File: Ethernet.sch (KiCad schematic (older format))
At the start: 2 parts, among them J2 RJMG2012211A0FR, U4 DP83869HMRGZT

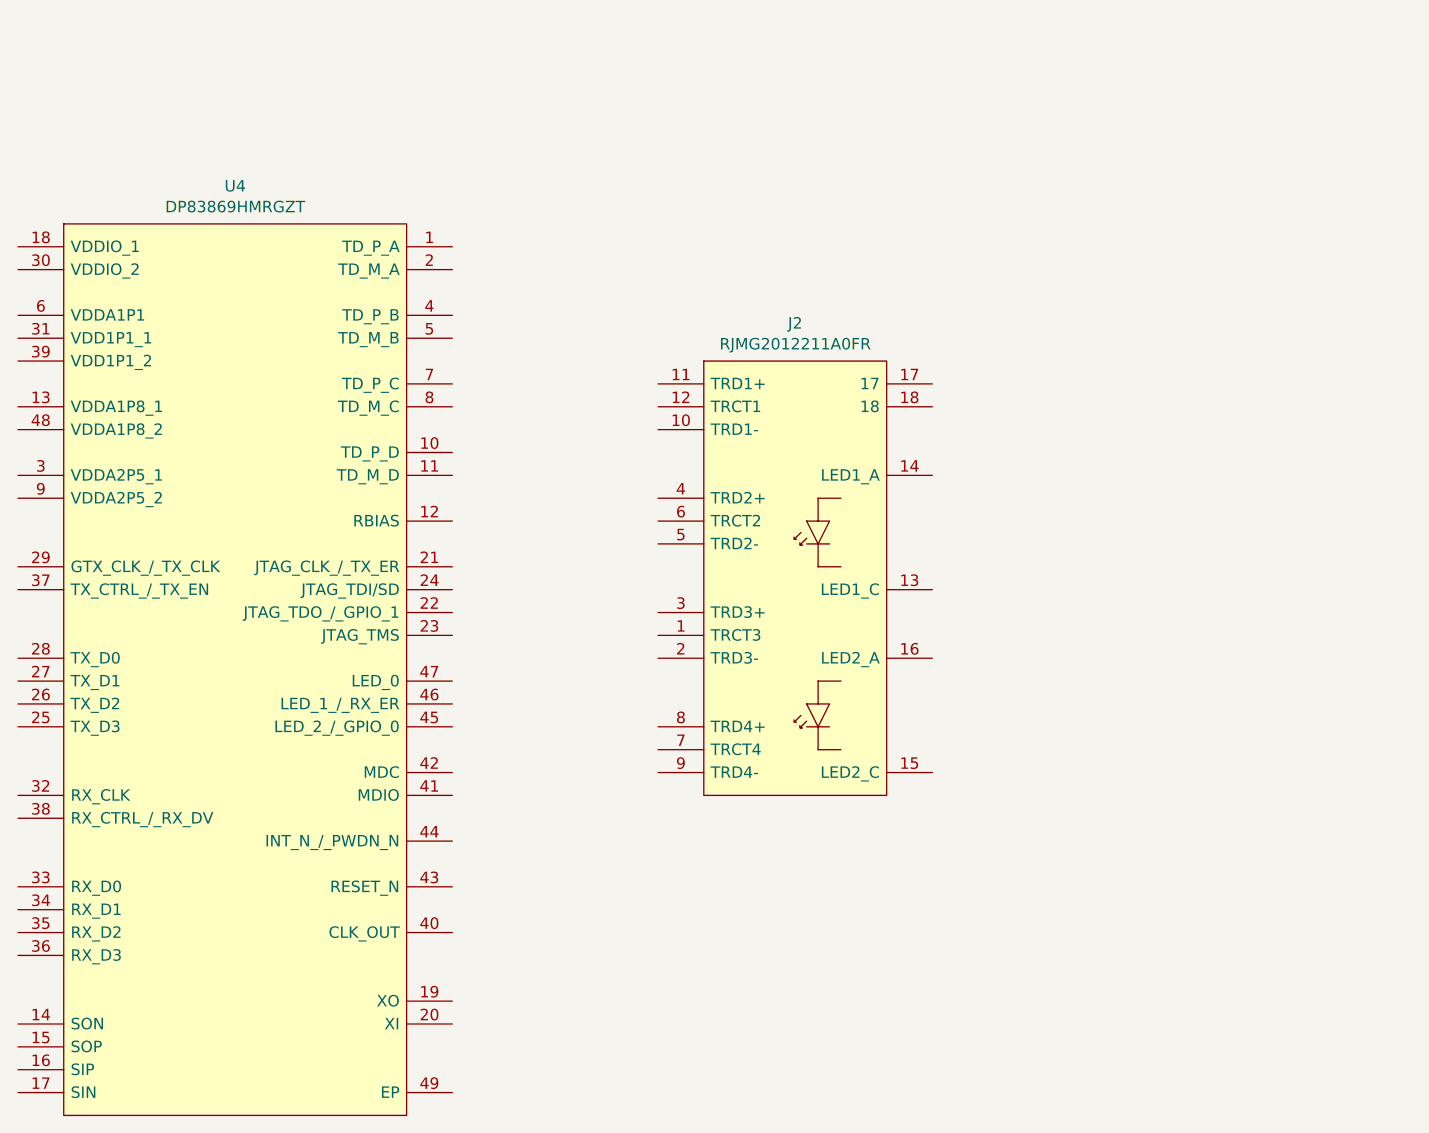
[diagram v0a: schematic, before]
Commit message: Added new sheet for Ethernet PHY Connector and drawn schematic (continue)
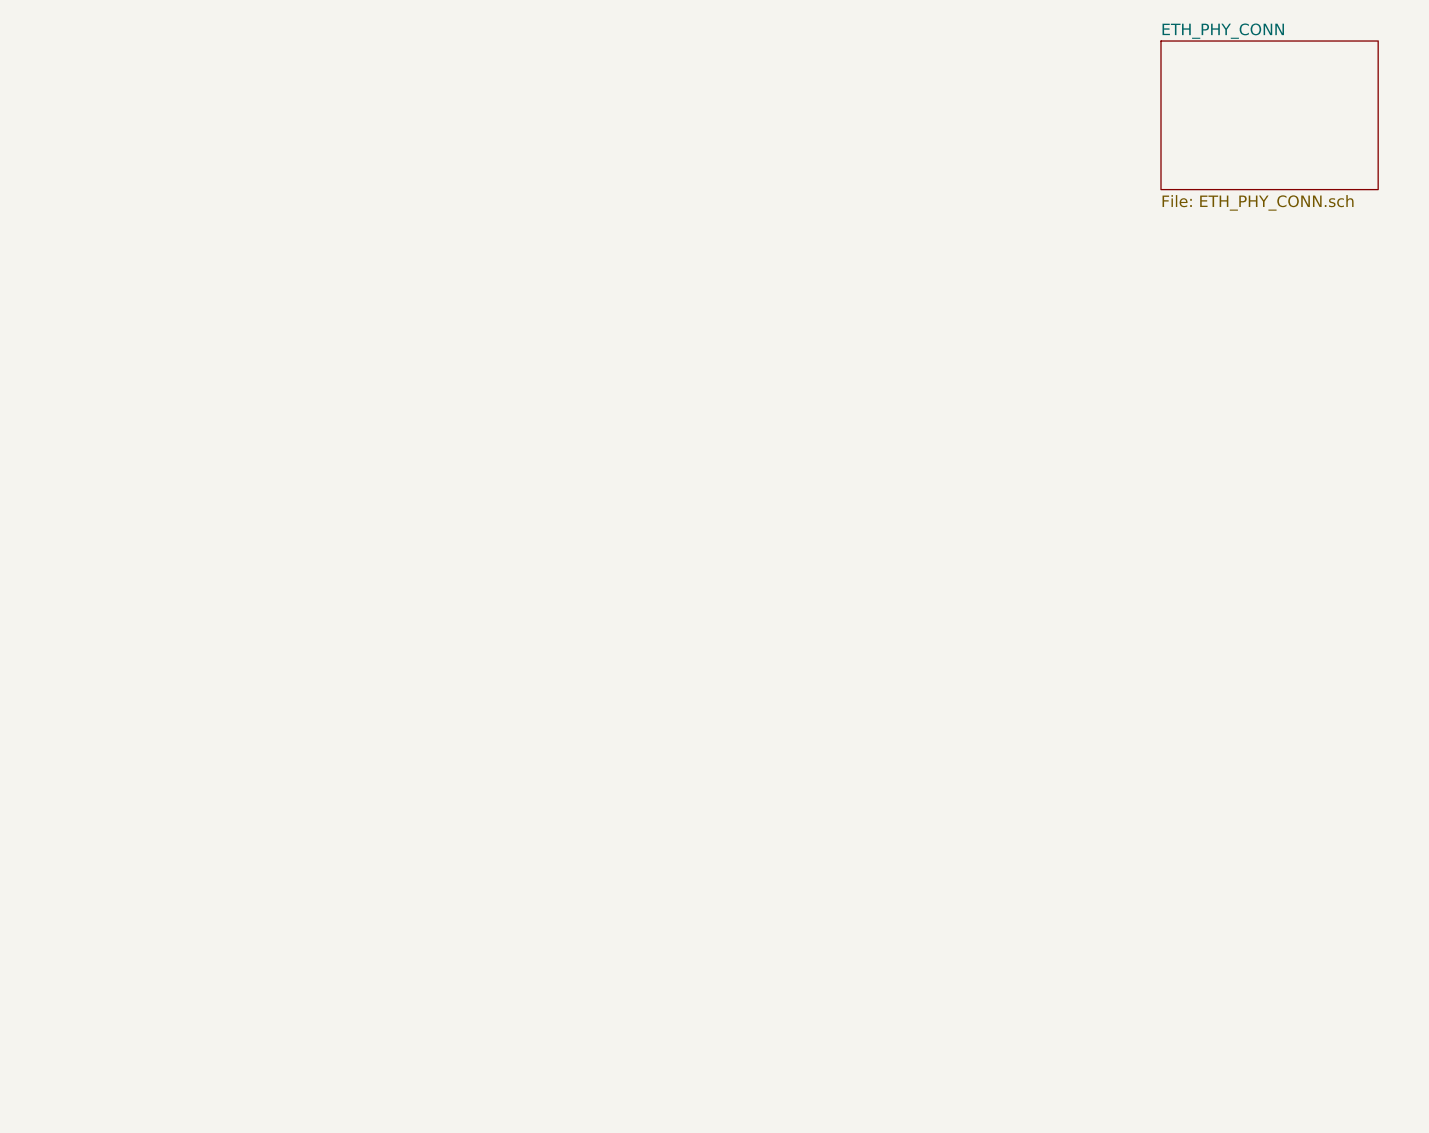
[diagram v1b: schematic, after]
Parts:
- removed J2: RJMG2012211A0FR, Connector_RJ:RJ45_Amphenol_RJMG2012211A0FR, symbol GM_Connectors:RJMG2012211A0FR
- removed U4: DP83869HMRGZT, QFN50P700X700X100-49N-D, symbol GM_Interface_IC:DP83869HMRGZT
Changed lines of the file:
@@
 $Descr A4 11693 8268
 encoding utf-8
-Sheet 11 14
+Sheet 11 15
 Title "CGMPCX1006"
 Date "2021-02-03"
@@
 Comment4 ""
 $EndDescr
-$Comp
-L GM_Connectors:RJMG2012211A0FR J2
-U 1 1 601C9357
-P 7900 2300
-F 0 "J2" H 8300 2465 50  0000 C CNN
-F 1 "RJMG2012211A0FR" H 8300 2374 50  0000 C CNN
-F 2 "Connector_RJ:RJ45_Amphenol_RJMG2012211A0FR" H 9650 2000 50  0001 L CNN
-F 3 "https://cdn.amphenol-icc.com/media/wysiwyg/files/drawing/rjmg2012211a0fr.pdf?__cf_chl_jschl_tk__=5cc0c62f4c4dd1ea6123210829694b2e9dccd0ec-1611686655-0-AbgBvwWp3czzY2TJ0ufJlAIwRl1VXRL4dc53SNg87JU7ShGwndvQnogLdV7Mq2dYunHoQquHJsd7cqqgMDrOCuNnWSljlLOxvZjuWQhC782DzE7hT4o80MjFt4sxGI4f_TcHgfVPuhccmcslPxq7SFrSDqxMMzQN2LDgsyEn_3ccqG3s2uHOZ2TkEeirzi6FrStejh0zz-mYYMOJCy1xpbmAF_0CAQpDLdH_WiZpwToopGmberC5N0wyHm6XbfAZEGelJSep-OdlFNMkB6nmqKb8TAkP2NiiS7GCJMgfNu5ZBovHLyUKdEt6EilXMFd55og80AbueHGldAWIFm-2Z3bJPHamRmYij0aInI9IGAYpuaLA_0nT0TMWXQY6i8JB94etuVIFkjYSa3PI-kWldruV9iNZxoLQLwTfUrN2H5nslIXfuzo0o-iOBHlw1zAeiQ" H 7250 3500 50  0001 L CNN
-	1    7900 2300
-	1    0    0    -1
-$EndComp
-$Comp
-L GM_Interface_IC:DP83869HMRGZT U4
-U 1 1 601CAF41
-P 5100 1700
-F 0 "U4" H 5850 1865 50  0000 C CNN
-F 1 "DP83869HMRGZT" H 5850 1774 50  0000 C CNN
-F 2 "QFN50P700X700X100-49N-D" H 8650 800 50  0001 L CNN
-F 3 "http://www.ti.com/lit/gpn/DP83869HM" H 8650 700 50  0001 L CNN
-	1    5100 1700
-	1    0    0    -1
-$EndComp
+$Sheet
+S 9900 900  950  650
+U 60257FE5
+F0 "ETH_PHY_CONN" 50
+F1 "ETH_PHY_CONN.sch" 50
+$EndSheet
 $EndSCHEMATC

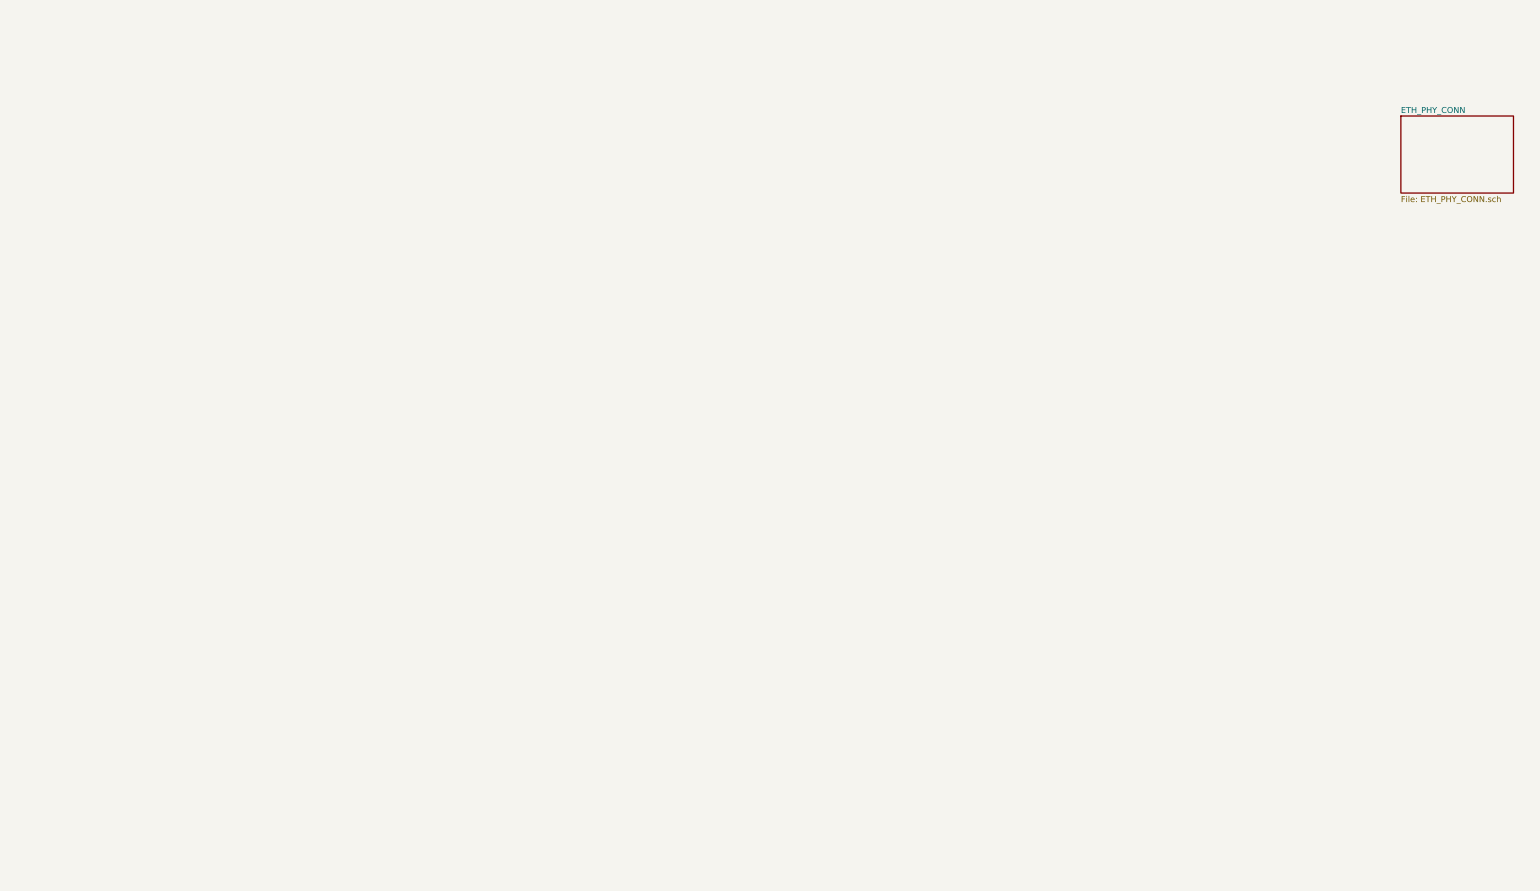
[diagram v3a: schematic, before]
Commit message: Drawn Eth power schematics and Eth PHY (continue)
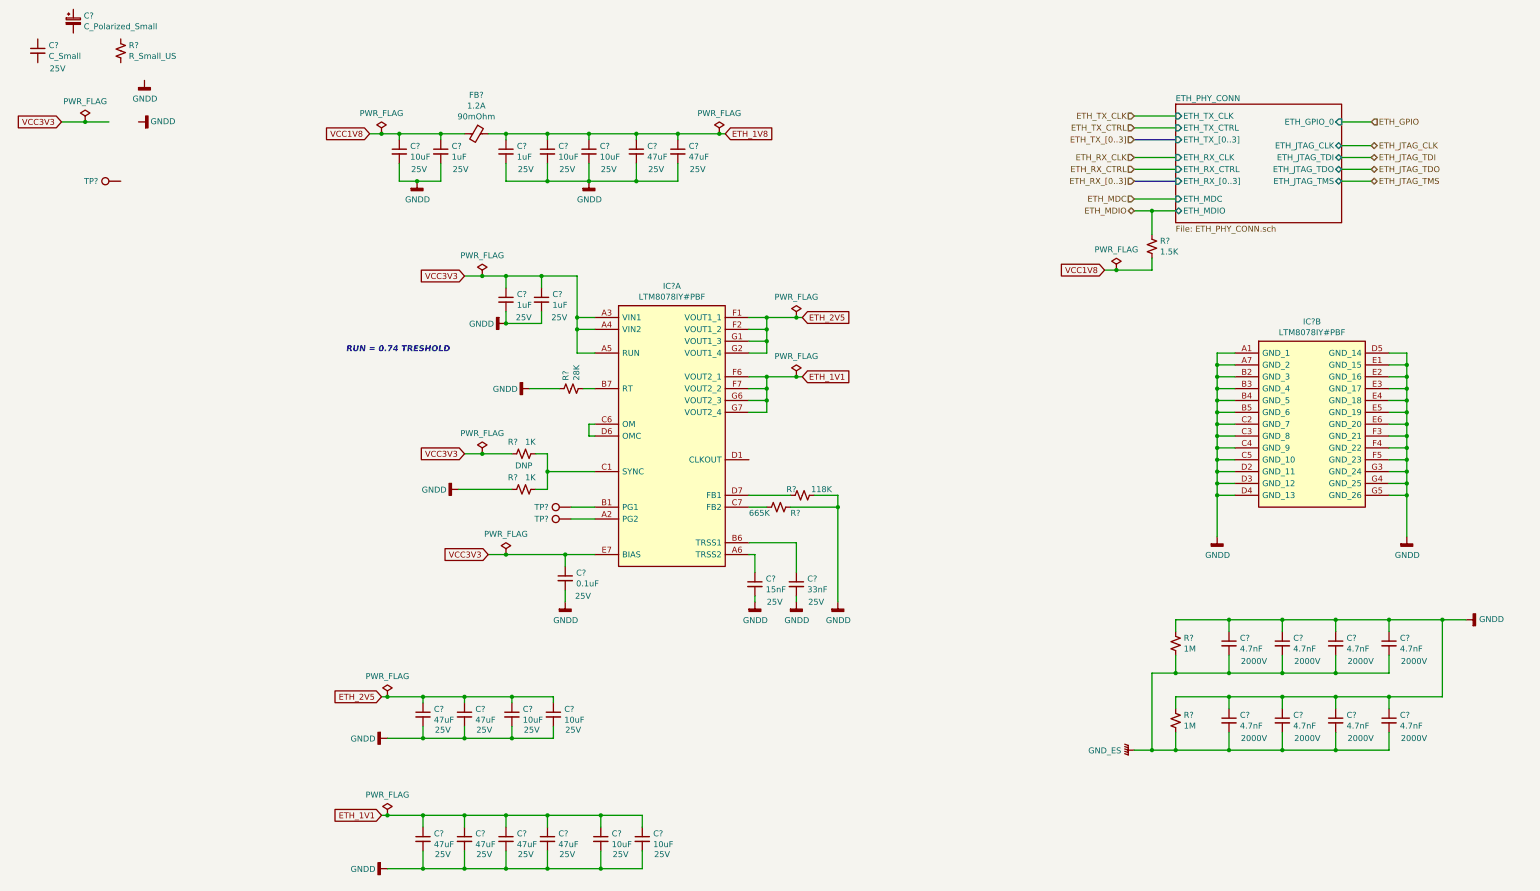
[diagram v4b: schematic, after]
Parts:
- added C?: C_Small, Capacitor_SMD:C_0603_1608Metric_Pad1.08x0.95mm_HandSolder, symbol Device:C_Small
- added C?: C_Polarized_Small, Capacitor_Tantalum_SMD:CP_EIA-1608-10_AVX-L_Pad1.25x1.05mm_HandSolder, symbol Device:C_Polarized_Small
- added C? (x4): 1uF, Capacitor_SMD:C_0603_1608Metric_Pad1.08x0.95mm_HandSolder, symbol Device:C_Small
- added C?: 0.1uF, Capacitor_SMD:C_0603_1608Metric_Pad1.08x0.95mm_HandSolder, symbol Device:C_Small
- added C?: 15nF, Capacitor_SMD:C_0603_1608Metric_Pad1.08x0.95mm_HandSolder, symbol Device:C_Small
- added C?: 33nF, Capacitor_SMD:C_0603_1608Metric_Pad1.08x0.95mm_HandSolder, symbol Device:C_Small
- added C? (x8): 47uF, Capacitor_SMD:C_0603_1608Metric_Pad1.08x0.95mm_HandSolder, symbol Device:C_Small
- added C? (x7): 10uF, Capacitor_SMD:C_0603_1608Metric_Pad1.08x0.95mm_HandSolder, symbol Device:C_Small
- added C? (x8): 4.7nF, Capacitor_SMD:C_0603_1608Metric_Pad1.08x0.95mm_HandSolder, symbol Device:C_Small
- added FB?: 1.2A, GM_Filter:BEADC1005X55N, symbol Device:FerriteBead_Small
- added IC? (x2): LTM8078IY#PBF, GM_BGA:BGA49C80P7X7_625X625X242, symbol GM_Voltage_Regulators:LTM8078IY#PBF
- added R?: R_Small_US, Resistor_SMD:R_0603_1608Metric_Pad0.98x0.95mm_HandSolder, symbol Device:R_Small_US
- added R?: 28K, Resistor_SMD:R_0603_1608Metric_Pad0.98x0.95mm_HandSolder, symbol Device:R_Small_US
- added R? (x2): 1K, Resistor_SMD:R_0603_1608Metric_Pad0.98x0.95mm_HandSolder, symbol Device:R_Small_US
- added R?: 665K, Resistor_SMD:R_0603_1608Metric_Pad0.98x0.95mm_HandSolder, symbol Device:R_Small_US
- added R?: 118K, Resistor_SMD:R_0603_1608Metric_Pad0.98x0.95mm_HandSolder, symbol Device:R_Small_US
- added R? (x2): 1M, Resistor_SMD:R_0603_1608Metric_Pad0.98x0.95mm_HandSolder, symbol Device:R_Small_US
- added R?: 1.5K, Resistor_SMD:R_0603_1608Metric_Pad0.98x0.95mm_HandSolder, symbol Device:R_Small_US
- added TP? (x3): TestPoint, TestPoint:TestPoint_Pad_D1.5mm, symbol Connector:TestPoint
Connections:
- new net: IC?.A2 (PG2), TP?.1
- new net: C?.1, IC?.A6 (TRSS2)
- new net: IC?.B1 (PG1), TP?.1
- new net: C?.1, IC?.B6 (TRSS1)
- new net: IC?.B7 (RT), R?.2
- new net: IC?.C1 (SYNC), R?.2, R?.2
- new net: IC?.C6 (OM), IC?.D6 (OMC)
- new net: IC?.C7 (FB2), R?.2
- new net: IC?.D7 (FB1), R?.1
- new net ETH_1V1: C?.1, C?.1, C?.1, C?.1, C?.1, C?.1, IC?.F6 (VOUT2_1), IC?.F7 (VOUT2_2), IC?.G6 (VOUT2_3), IC?.G7 (VOUT2_4)
- new net ETH_1V8: C?.1, C?.1, C?.1, C?.1, C?.1, FB?.1
- new net ETH_2V5: C?.1, C?.1, C?.1, C?.1, IC?.F1 (VOUT1_1), IC?.F2 (VOUT1_2), IC?.G1 (VOUT1_3), IC?.G2 (VOUT1_4)
- new net ETH_MDIO: R?.1
- new net GNDD: C?.1, C?.1, C?.1, C?.1, C?.1, C?.1, C?.1, C?.1, C?.2, C?.2, C?.2, C?.2, C?.2, C?.2, C?.2, C?.2, C?.2, C?.2, C?.2, C?.2, C?.2, C?.2, C?.2, C?.2, C?.2, C?.2, C?.2, C?.2, C?.2, C?.2, IC?.A1 (GND_1), IC?.A7 (GND_2), IC?.B2 (GND_3), IC?.B3 (GND_4), IC?.B4 (GND_5), IC?.B5 (GND_6), IC?.C2 (GND_7), IC?.C3 (GND_8), IC?.C4 (GND_9), IC?.C5 (GND_10), IC?.D2 (GND_11), IC?.D3 (GND_12), IC?.D4 (GND_13), IC?.D5 (GND_14), IC?.E1 (GND_15), IC?.E2 (GND_16), IC?.E3 (GND_17), IC?.E4 (GND_18), IC?.E5 (GND_19), IC?.E6 (GND_20), IC?.F3 (GND_21), IC?.F4 (GND_22), IC?.F5 (GND_23), IC?.G3 (GND_24), IC?.G4 (GND_25), IC?.G5 (GND_26), R?.1, R?.1, R?.1, R?.1, R?.1, R?.2
- new net GND_ES: C?.2, C?.2, C?.2, C?.2, C?.2, C?.2, C?.2, C?.2, R?.2, R?.2
- new net VCC1V8: C?.1, C?.1, FB?.2, R?.2
- new net VCC3V3: C?.1, C?.1, C?.1, IC?.A3 (VIN1), IC?.A4 (VIN2), IC?.A5 (RUN), IC?.E7 (BIAS), R?.1
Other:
- note added: "RUN = 0.74 TRESHOLD\n"

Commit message: Drawn Ethernet PHY schematics
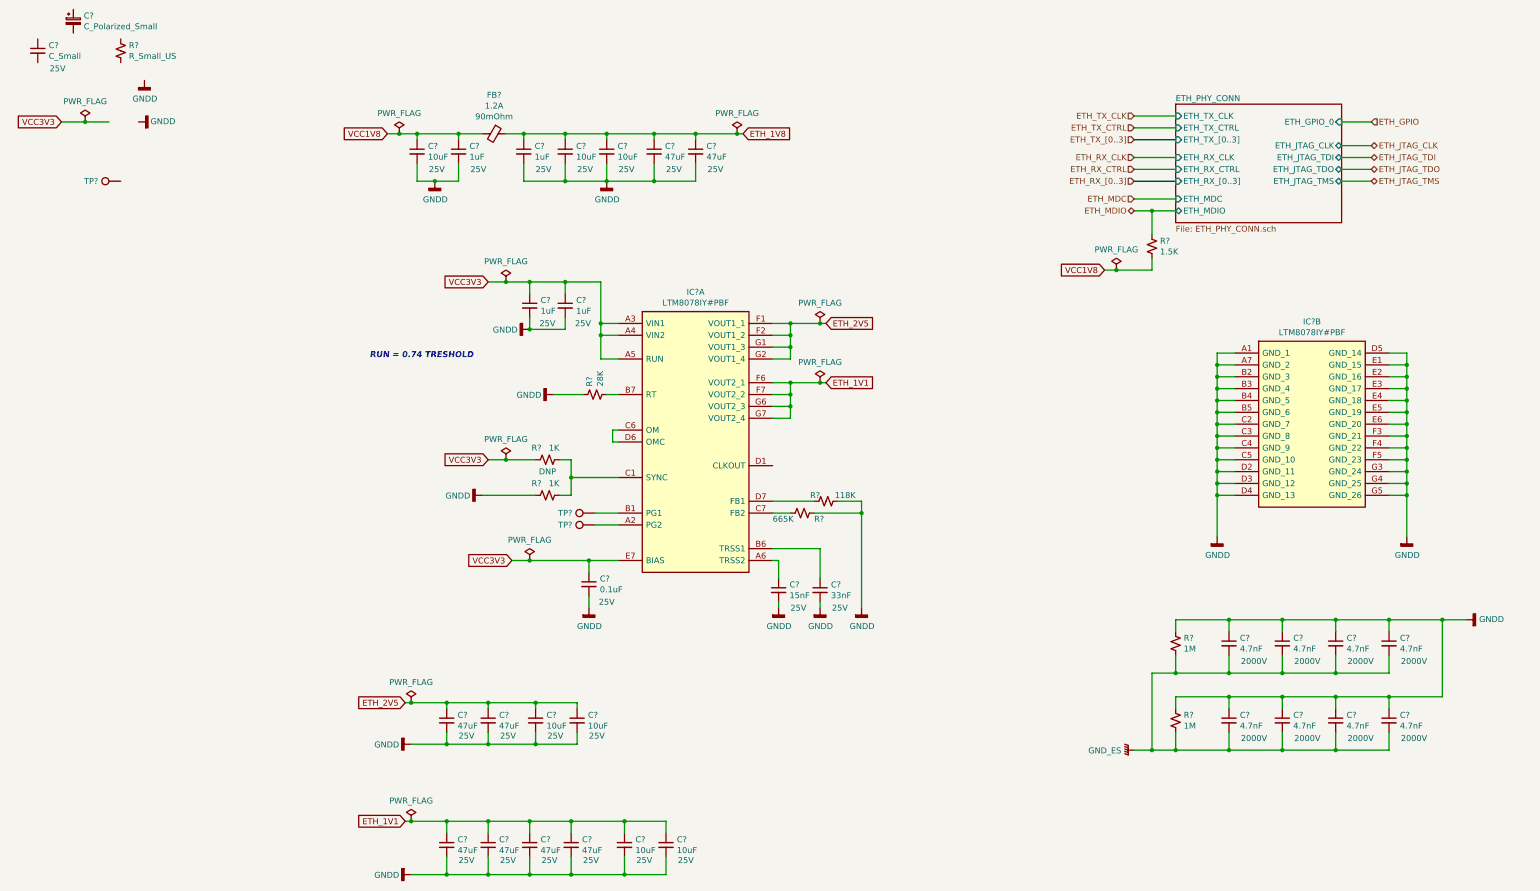
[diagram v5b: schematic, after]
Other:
- moved on the sheet: C?, FB?, IC?A, R?, TP?
